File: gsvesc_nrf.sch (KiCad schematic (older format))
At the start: 2 parts

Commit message: SCM Fertig
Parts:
- J14: renamed from J?; footprint (none) -> Connector_PinHeader_2.54mm:PinHeader_2x04_P2.54mm_Vertical
- R41: renamed from R?; value R -> 10K0; footprint (none) -> Resistor_SMD:R_0805_2012Metric
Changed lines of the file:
@@
 $EndDescr
 $Comp
-L Connector_Generic:Conn_02x04_Odd_Even J?
+L Connector_Generic:Conn_02x04_Odd_Even J14
 U 1 1 5C039131
 P 4850 2900
-F 0 "J?" H 4900 3217 50  0000 C CNN
+F 0 "J14" H 4900 3217 50  0000 C CNN
 F 1 "Conn_02x04_Odd_Even" H 4900 3126 50  0000 C CNN
-F 2 "" H 4850 2900 50  0001 C CNN
+F 2 "Connector_PinHeader_2.54mm:PinHeader_2x04_P2.54mm_Vertical" H 4850 2900 50  0001 C CNN
 F 3 "~" H 4850 2900 50  0001 C CNN
 	1    4850 2900
@@
 NRF Connector\n
 $Comp
-L Device:R R?
+L Device:R R41
 U 1 1 5C0391EE
 P 4400 2900
-F 0 "R?" V 4350 2650 50  0000 C CNN
-F 1 "R" V 4400 2850 50  0000 C CNN
-F 2 "" V 4330 2900 50  0001 C CNN
+F 0 "R41" V 4350 2650 50  0000 C CNN
+F 1 "10K0" V 4400 2850 50  0000 C CNN
+F 2 "Resistor_SMD:R_0805_2012Metric" V 4330 2900 50  0001 C CNN
 F 3 "~" H 4400 2900 50  0001 C CNN
 	1    4400 2900
@@
 	4050 2800 4650 2800
 $Comp
-L power:GND #PWR?
+L power:GND #PWR064
 U 1 1 5C03930C
 P 4050 2800
-F 0 "#PWR?" H 4050 2550 50  0001 C CNN
+F 0 "#PWR064" H 4050 2550 50  0001 C CNN
 F 1 "GND" V 4055 2672 50  0000 R CNN
 F 2 "" H 4050 2800 50  0001 C CNN
@@
 $EndComp
 $Comp
-L power:VCC #PWR?
+L power:VCC #PWR065
 U 1 1 5C03933D
 P 5650 2800
-F 0 "#PWR?" H 5650 2650 50  0001 C CNN
+F 0 "#PWR065" H 5650 2650 50  0001 C CNN
 F 1 "VCC" V 5667 2928 50  0000 L CNN
 F 2 "" H 5650 2800 50  0001 C CNN
@@
 	4250 2900 4000 2900
 $Comp
-L power:VCC #PWR?
+L power:VCC #PWR063
 U 1 1 5C03946B
 P 4000 2900
-F 0 "#PWR?" H 4000 2750 50  0001 C CNN
+F 0 "#PWR063" H 4000 2750 50  0001 C CNN
 F 1 "VCC" V 4018 3027 50  0000 L CNN
 F 2 "" H 4000 2900 50  0001 C CNN

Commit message: design finished gerber created
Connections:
- net SCK renamed SCLK
- no-connect marks 0 -> 1
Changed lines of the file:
@@
 MOSI
 Text HLabel 4000 3000 0    50   Input ~ 0
-SCK
+SCLK
 Text HLabel 4000 3100 0    50   Input ~ 0
 MISO
+NoConn ~ 5150 3100
 $EndSCHEMATC

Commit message: test
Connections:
- net labels added: NRF_RX, NRF_TX
- net labels removed: CS, MISO, MOSI, SCLK
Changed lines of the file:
@@
 Title "GSVESC - DC Motor Controler"
 Date "2018-11-11"
-Rev "2.0"
+Rev "3.0"
 Comp ""
 Comment1 ""
@@
 Wire Wire Line
 	5150 3000 5700 3000
-Text HLabel 5700 2900 2    50   Input ~ 0
-CS
-Text HLabel 5700 3000 2    50   Input ~ 0
-MOSI
+NoConn ~ 5150 3100
 Text HLabel 4000 3000 0    50   Input ~ 0
-SCLK
+NRF_TX
 Text HLabel 4000 3100 0    50   Input ~ 0
-MISO
-NoConn ~ 5150 3100
+NRF_RX
 $EndSCHEMATC

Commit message: gsesc v3, work in progress
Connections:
- net labels added: GPIO1, GPIO2, GPIO3
- wire segments 8 -> 9
- no-connect marks 1 -> 0
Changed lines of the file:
@@
 $Descr A4 11693 8268
 encoding utf-8
-Sheet 6 6
-Title "GSVESC - DC Motor Controler"
+Sheet 5 5
+Title "GSESC - DC Motor Controler"
 Date "2018-11-11"
 Rev "3.0"
@@
 Comment4 ""
 $EndDescr
-$Comp
-L Connector_Generic:Conn_02x04_Odd_Even J14
-U 1 1 5C039131
-P 4850 2900
-F 0 "J14" H 4900 3217 50  0000 C CNN
-F 1 "Conn_02x04_Odd_Even" H 4900 3126 50  0000 C CNN
-F 2 "Connector_PinHeader_2.54mm:PinHeader_2x04_P2.54mm_Vertical" H 4850 2900 50  0001 C CNN
-F 3 "~" H 4850 2900 50  0001 C CNN
-	1    4850 2900
-	1    0    0    -1
-$EndComp
 Text Notes 8950 6900 2    157  ~ 0
 NRF Connector\n
@@
 Wire Wire Line
 	4650 3000 4000 3000
-Wire Wire Line
-	5150 2900 5700 2900
-Wire Wire Line
-	5150 3000 5700 3000
-NoConn ~ 5150 3100
 Text HLabel 4000 3000 0    50   Input ~ 0
 NRF_TX
 Text HLabel 4000 3100 0    50   Input ~ 0
 NRF_RX
+Text HLabel 5300 2900 2    50   Input ~ 0
+GPIO1
+$Comp
+L Connector_Generic:Conn_02x04_Odd_Even J14
+U 1 1 5C039131
+P 4850 2900
+F 0 "J14" H 4900 3217 50  0000 C CNN
+F 1 "Conn_02x04_Odd_Even" H 4900 3126 50  0000 C CNN
+F 2 "Connector_PinHeader_2.54mm:PinHeader_2x04_P2.54mm_Vertical" H 4850 2900 50  0001 C CNN
+F 3 "~" H 4850 2900 50  0001 C CNN
+	1    4850 2900
+	1    0    0    -1
+$EndComp
+Wire Wire Line
+	5300 2900 5150 2900
+Text HLabel 5300 3000 2    50   Input ~ 0
+GPIO2
+Text HLabel 5300 3100 2    50   Input ~ 0
+GPIO3
+Wire Wire Line
+	5300 3000 5150 3000
+Wire Wire Line
+	5300 3100 5150 3100
 $EndSCHEMATC

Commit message: V4 alpha
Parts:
- R41: value 10K0 -> 10k0
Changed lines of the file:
@@
 P 4400 2900
 F 0 "R41" V 4350 2650 50  0000 C CNN
-F 1 "10K0" V 4400 2850 50  0000 C CNN
+F 1 "10k0" V 4400 2850 50  0000 C CNN
 F 2 "Resistor_SMD:R_0805_2012Metric" V 4330 2900 50  0001 C CNN
 F 3 "~" H 4400 2900 50  0001 C CNN

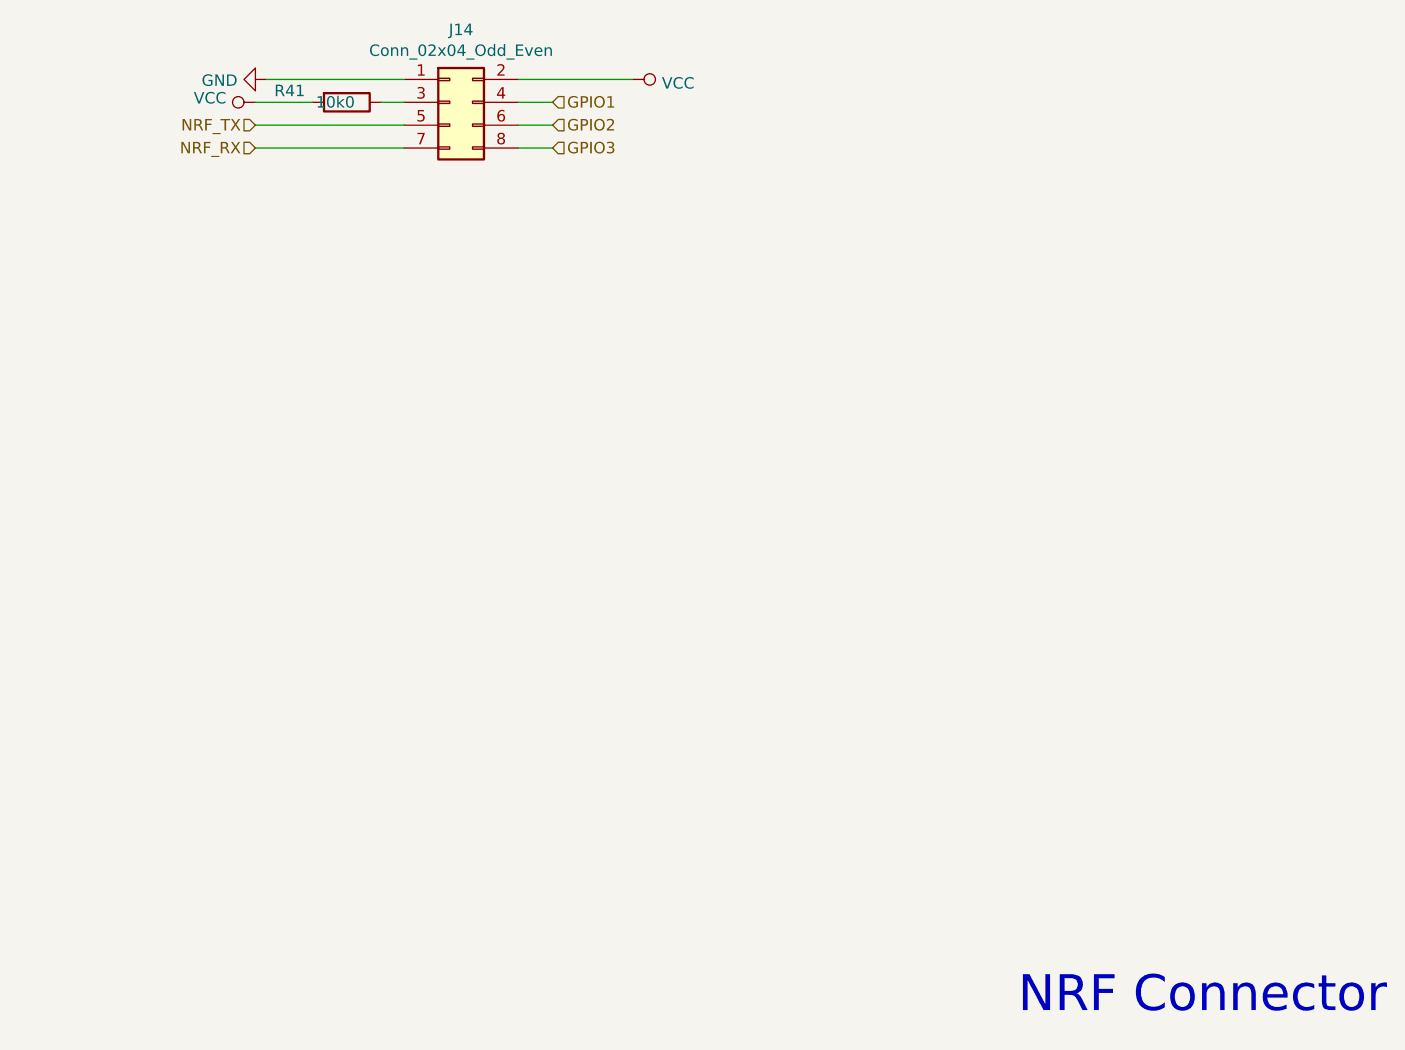
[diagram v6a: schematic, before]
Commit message: BLE Modul hinzugefügt, optional
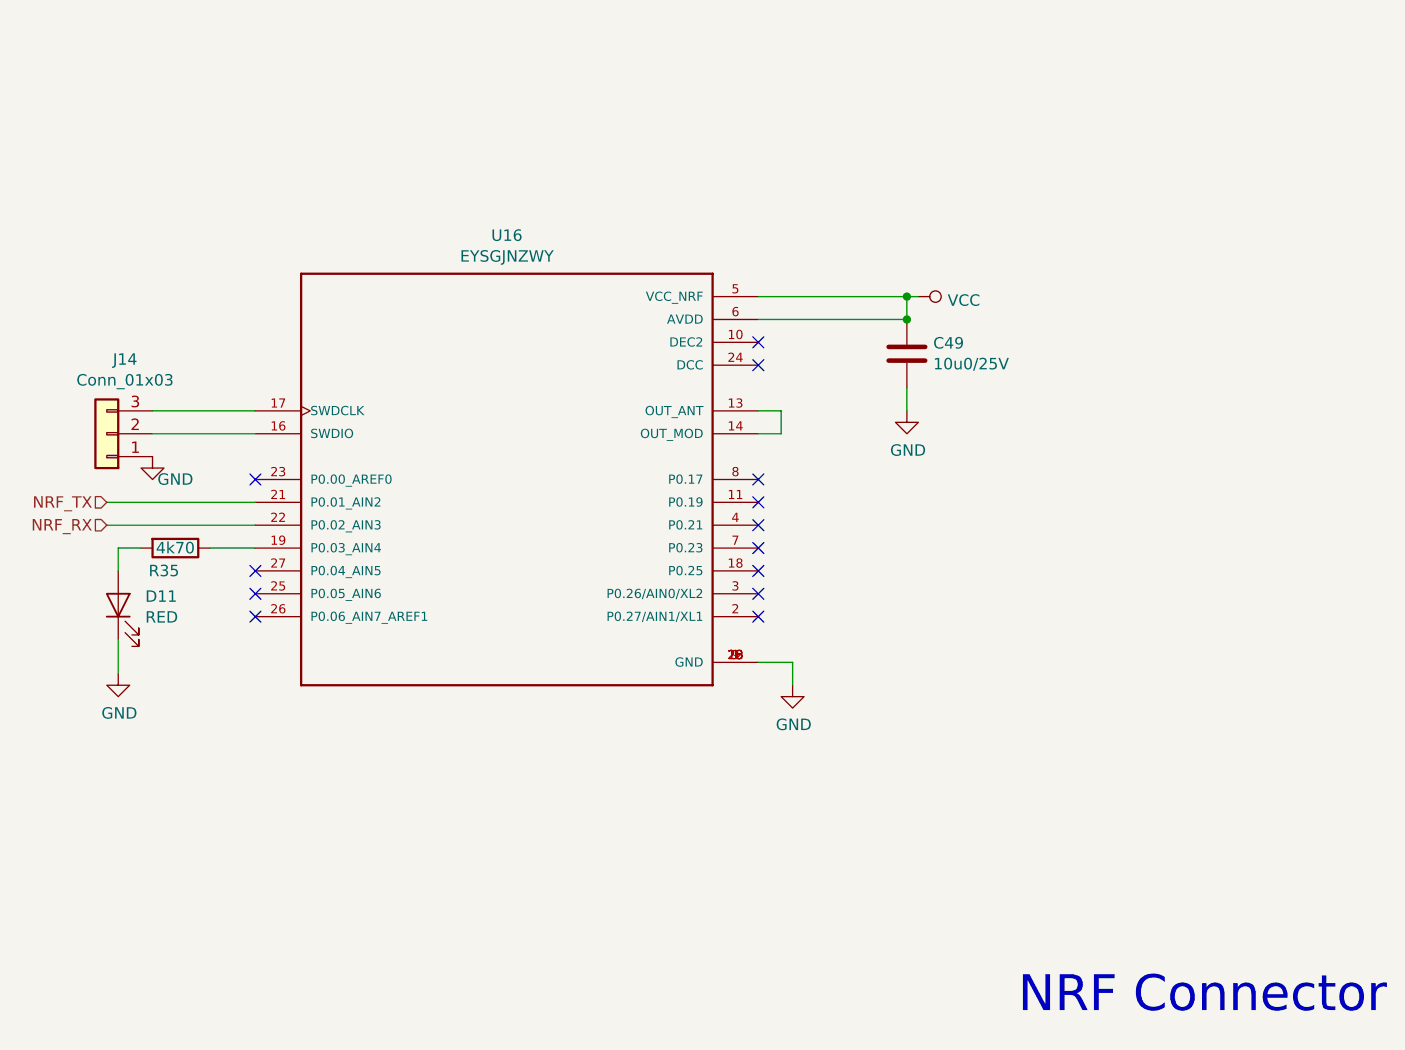
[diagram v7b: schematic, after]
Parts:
- removed J14: Conn_02x04_Odd_Even, Connector_PinHeader_2.54mm:PinHeader_2x04_P2.54mm_Vertical, symbol Connector_Generic:Conn_02x04_Odd_Even
- removed R41: 10k0, Resistor_SMD:R_0805_2012Metric, symbol Device:R
- added C49: 10u0/25V, Capacitor_SMD:C_0805_2012Metric, symbol Device:C
- added D11: RED, LED_SMD:LED_0805_2012Metric, symbol Device:LED
- added J14: Conn_01x03, Connector_JST:JST_SH_BM03B-SRSS-TB_1x03-1MP_P1.00mm_Vertical, symbol Connector_Generic:Conn_01x03
- added R35: 4k70, Resistor_SMD:R_0805_2012Metric, symbol Device:R
- added U16: EYSGJNZWY, gsvesc:BLE_EYSGJNZWY, symbol gsvesc:EYSGJNZWY
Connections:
- net GND: now also C49.2, D11.1 (K), J14.1 (Pin_1), U16.1 (GND), U16.12 (GND), U16.15 (GND), U16.20 (GND), U16.28 (GND), U16.9 (GND)
- net NRF_RX: now also U16.22 (P0.02_AIN3)
- net NRF_TX: now also U16.21 (P0.01_AIN2)
- net VCC: now also C49.1, U16.5 (VCC_NRF), U16.6 (AVDD)
- new net: U16.13 (OUT_ANT), U16.14 (OUT_MOD)
- new net: J14.2 (Pin_2), U16.16 (SWDIO)
- new net: J14.3 (Pin_3), U16.17 (SWDCLK)
- new net: R35.1, U16.19 (P0.03_AIN4)
- new net: D11.2 (A), R35.2
- no-connect marks 0 -> 13
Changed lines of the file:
@@
 NRF Connector\n
 $Comp
-L Device:R R41
-U 1 1 5C0391EE
-P 4400 2900
-F 0 "R41" V 4350 2650 50  0000 C CNN
-F 1 "10k0" V 4400 2850 50  0000 C CNN
-F 2 "Resistor_SMD:R_0805_2012Metric" V 4330 2900 50  0001 C CNN
-F 3 "~" H 4400 2900 50  0001 C CNN
-	1    4400 2900
+L power:VCC #PWR065
+U 1 1 5C03933D
+P 6900 3750
+F 0 "#PWR065" H 6900 3600 50  0001 C CNN
+F 1 "VCC" V 6917 3878 50  0000 L CNN
+F 2 "" H 6900 3750 50  0001 C CNN
+F 3 "" H 6900 3750 50  0001 C CNN
+	1    6900 3750
 	0    1    1    0
 $EndComp
 Wire Wire Line
-	4050 2800 4650 2800
+	4000 4750 3350 4750
+Wire Wire Line
+	4000 4650 3350 4650
+Text HLabel 3350 4650 0    50   Input ~ 0
+NRF_TX
+Text HLabel 3350 4750 0    50   Input ~ 0
+NRF_RX
 $Comp
-L power:GND #PWR064
-U 1 1 5C03930C
-P 4050 2800
-F 0 "#PWR064" H 4050 2550 50  0001 C CNN
-F 1 "GND" V 4055 2672 50  0000 R CNN
-F 2 "" H 4050 2800 50  0001 C CNN
-F 3 "" H 4050 2800 50  0001 C CNN
-	1    4050 2800
-	0    1    1    0
+L gsvesc:EYSGJNZWY U16
+U 1 1 5E9F870E
+P 5100 4550
+F 0 "U16" H 5100 5617 50  0000 C CNN
+F 1 "EYSGJNZWY" H 5100 5526 50  0000 C CNN
+F 2 "gsvesc:BLE_EYSGJNZWY" H 5100 4550 50  0001 L BNN
+F 3 "Manufacturer Recommendation" H 5100 4550 50  0001 L BNN
+F 4 "1.3" H 5100 4550 50  0001 L BNN "Field4"
+F 5 "Taiyo Yuden" H 5100 4550 50  0001 L BNN "Field5"
+	1    5100 4550
+	1    0    0    -1
 $EndComp
+Wire Wire Line
+	6200 3750 6850 3750
+Wire Wire Line
+	6200 3850 6850 3850
+Wire Wire Line
+	6850 3850 6850 3750
+Connection ~ 6850 3750
+Wire Wire Line
+	6850 3750 6900 3750
+NoConn ~ 6200 3950
+NoConn ~ 6200 4050
 $Comp
-L power:VCC #PWR065
-U 1 1 5C03933D
-P 5650 2800
-F 0 "#PWR065" H 5650 2650 50  0001 C CNN
-F 1 "VCC" V 5667 2928 50  0000 L CNN
-F 2 "" H 5650 2800 50  0001 C CNN
-F 3 "" H 5650 2800 50  0001 C CNN
-	1    5650 2800
+L Device:C C49
+U 1 1 5E9F8DF1
+P 6850 4000
+F 0 "C49" H 6965 4046 50  0000 L CNN
+F 1 "10u0/25V" H 6965 3955 50  0000 L CNN
+F 2 "Capacitor_SMD:C_0805_2012Metric" H 6888 3850 50  0001 C CNN
+F 3 "~" H 6850 4000 50  0001 C CNN
+	1    6850 4000
+	1    0    0    -1
+$EndComp
+Connection ~ 6850 3850
+$Comp
+L power:GND #PWR0155
+U 1 1 5E9F8E5E
+P 6850 4250
+F 0 "#PWR0155" H 6850 4000 50  0001 C CNN
+F 1 "GND" H 6855 4077 50  0000 C CNN
+F 2 "" H 6850 4250 50  0001 C CNN
+F 3 "" H 6850 4250 50  0001 C CNN
+	1    6850 4250
+	1    0    0    -1
+$EndComp
+Wire Wire Line
+	6850 4250 6850 4150
+Wire Wire Line
+	6200 4250 6300 4250
+Wire Wire Line
+	6300 4250 6300 4350
+Wire Wire Line
+	6300 4350 6200 4350
+$Comp
+L Device:R R35
+U 1 1 5E9F90E0
+P 3650 4850
+F 0 "R35" V 3750 4800 50  0000 C CNN
+F 1 "4k70" V 3650 4850 50  0000 C CNN
+F 2 "Resistor_SMD:R_0805_2012Metric" V 3580 4850 50  0001 C CNN
+F 3 "~" H 3650 4850 50  0001 C CNN
+	1    3650 4850
 	0    1    1    0
 $EndComp
 Wire Wire Line
-	4650 3100 4000 3100
-Wire Wire Line
-	4650 2900 4550 2900
-Wire Wire Line
-	4250 2900 4000 2900
+	4000 4850 3800 4850
 $Comp
-L power:VCC #PWR063
-U 1 1 5C03946B
-P 4000 2900
-F 0 "#PWR063" H 4000 2750 50  0001 C CNN
-F 1 "VCC" V 4018 3027 50  0000 L CNN
-F 2 "" H 4000 2900 50  0001 C CNN
-F 3 "" H 4000 2900 50  0001 C CNN
-	1    4000 2900
+L Device:LED D11
+U 1 1 5E9F93A3
+P 3400 5100
+F 0 "D11" V 3438 4982 50  0000 R CNN
+F 1 "RED" V 3347 4982 50  0000 R CNN
+F 2 "LED_SMD:LED_0805_2012Metric" H 3400 5100 50  0001 C CNN
+F 3 "~" H 3400 5100 50  0001 C CNN
+	1    3400 5100
 	0    -1   -1   0
 $EndComp
 Wire Wire Line
-	5150 2800 5650 2800
+	3500 4850 3400 4850
 Wire Wire Line
-	4650 3000 4000 3000
-Text HLabel 4000 3000 0    50   Input ~ 0
-NRF_TX
-Text HLabel 4000 3100 0    50   Input ~ 0
-NRF_RX
-Text HLabel 5300 2900 2    50   Input ~ 0
-GPIO1
+	3400 4850 3400 4950
 $Comp
-L Connector_Generic:Conn_02x04_Odd_Even J14
-U 1 1 5C039131
-P 4850 2900
-F 0 "J14" H 4900 3217 50  0000 C CNN
-F 1 "Conn_02x04_Odd_Even" H 4900 3126 50  0000 C CNN
-F 2 "Connector_PinHeader_2.54mm:PinHeader_2x04_P2.54mm_Vertical" H 4850 2900 50  0001 C CNN
-F 3 "~" H 4850 2900 50  0001 C CNN
-	1    4850 2900
+L power:GND #PWR0156
+U 1 1 5E9F967D
+P 3400 5400
+F 0 "#PWR0156" H 3400 5150 50  0001 C CNN
+F 1 "GND" H 3405 5227 50  0000 C CNN
+F 2 "" H 3400 5400 50  0001 C CNN
+F 3 "" H 3400 5400 50  0001 C CNN
+	1    3400 5400
 	1    0    0    -1
 $EndComp
 Wire Wire Line
-	5300 2900 5150 2900
-Text HLabel 5300 3000 2    50   Input ~ 0
-GPIO2
-Text HLabel 5300 3100 2    50   Input ~ 0
-GPIO3
+	3400 5400 3400 5250
+NoConn ~ 6200 4550
+NoConn ~ 6200 4650
+NoConn ~ 6200 4750
+NoConn ~ 6200 4850
+NoConn ~ 6200 4950
+NoConn ~ 6200 5050
+NoConn ~ 6200 5150
+NoConn ~ 4000 4950
+NoConn ~ 4000 5050
+NoConn ~ 4000 5150
+NoConn ~ 4000 4550
+$Comp
+L power:GND #PWR0157
+U 1 1 5E9FAD8C
+P 6350 5450
+F 0 "#PWR0157" H 6350 5200 50  0001 C CNN
+F 1 "GND" H 6355 5277 50  0000 C CNN
+F 2 "" H 6350 5450 50  0001 C CNN
+F 3 "" H 6350 5450 50  0001 C CNN
+	1    6350 5450
+	1    0    0    -1
+$EndComp
 Wire Wire Line
-	5300 3000 5150 3000
+	6200 5350 6350 5350
 Wire Wire Line
-	5300 3100 5150 3100
+	6350 5350 6350 5450
+$Comp
+L Connector_Generic:Conn_01x03 J14
+U 1 1 5E9FAF5C
+P 3350 4350
+F 0 "J14" H 3270 4025 50  0000 C CNN
+F 1 "Conn_01x03" H 3270 4116 50  0000 C CNN
+F 2 "Connector_JST:JST_SH_BM03B-SRSS-TB_1x03-1MP_P1.00mm_Vertical" H 3350 4350 50  0001 C CNN
+F 3 "~" H 3350 4350 50  0001 C CNN
+	1    3350 4350
+	-1   0    0    1
+$EndComp
+Wire Wire Line
+	4000 4350 3550 4350
+Wire Wire Line
+	3550 4250 4000 4250
+$Comp
+L power:GND #PWR0158
+U 1 1 5E9FB3BA
+P 3550 4450
+F 0 "#PWR0158" H 3550 4200 50  0001 C CNN
+F 1 "GND" H 3650 4350 50  0000 C CNN
+F 2 "" H 3550 4450 50  0001 C CNN
+F 3 "" H 3550 4450 50  0001 C CNN
+	1    3550 4450
+	1    0    0    -1
+$EndComp
 $EndSCHEMATC

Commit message: V4 before review
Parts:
- R35: value 4k70 -> 7k50
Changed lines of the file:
@@
 P 3650 4850
 F 0 "R35" V 3750 4800 50  0000 C CNN
-F 1 "4k70" V 3650 4850 50  0000 C CNN
+F 1 "7k50" V 3650 4850 50  0000 C CNN
 F 2 "Resistor_SMD:R_0805_2012Metric" V 3580 4850 50  0001 C CNN
 F 3 "~" H 3650 4850 50  0001 C CNN
